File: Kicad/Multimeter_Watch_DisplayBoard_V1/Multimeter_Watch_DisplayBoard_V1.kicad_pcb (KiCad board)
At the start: 2 copper layers, 55 x 46 mm, 19 parts, among them J1 Conn_01x03_Male, J2 Conn_01x03_Male, J3 Conn_01x03_Male, J4 Conn_01x03_Male, Q1 A03400A N-MOS, SW1 SW_Push, SW2 SW_Push, SW3 SW_Push, SW4 SW_Push, SW5 SW_Push, SW6 SW_Push

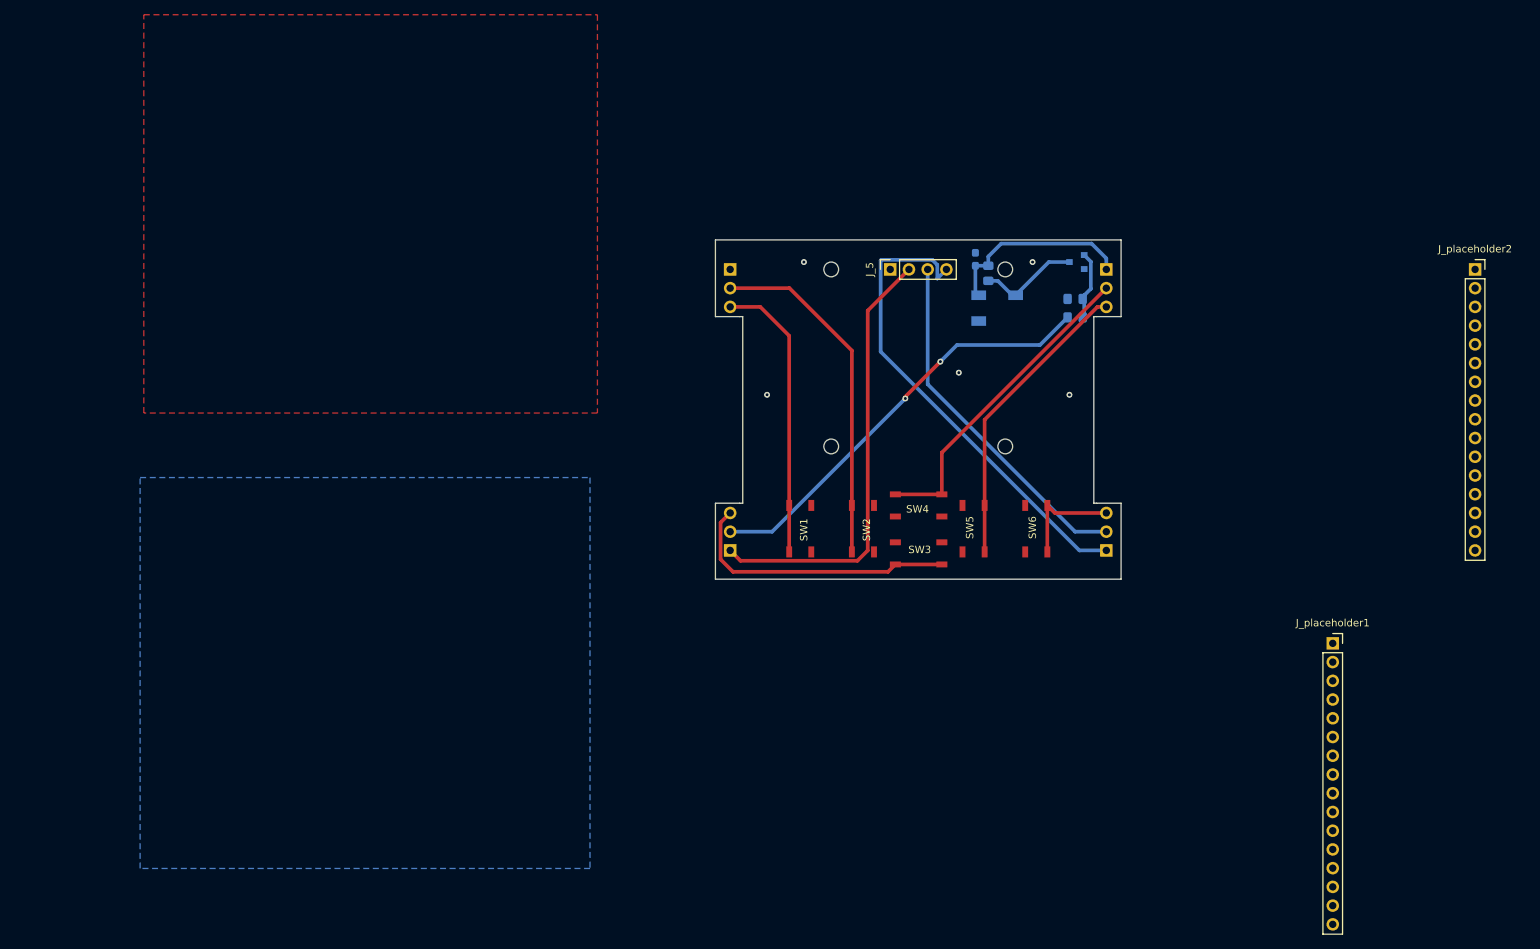
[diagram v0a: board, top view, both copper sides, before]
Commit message: display board laid out, added silkscreen desc. of pins and jacks
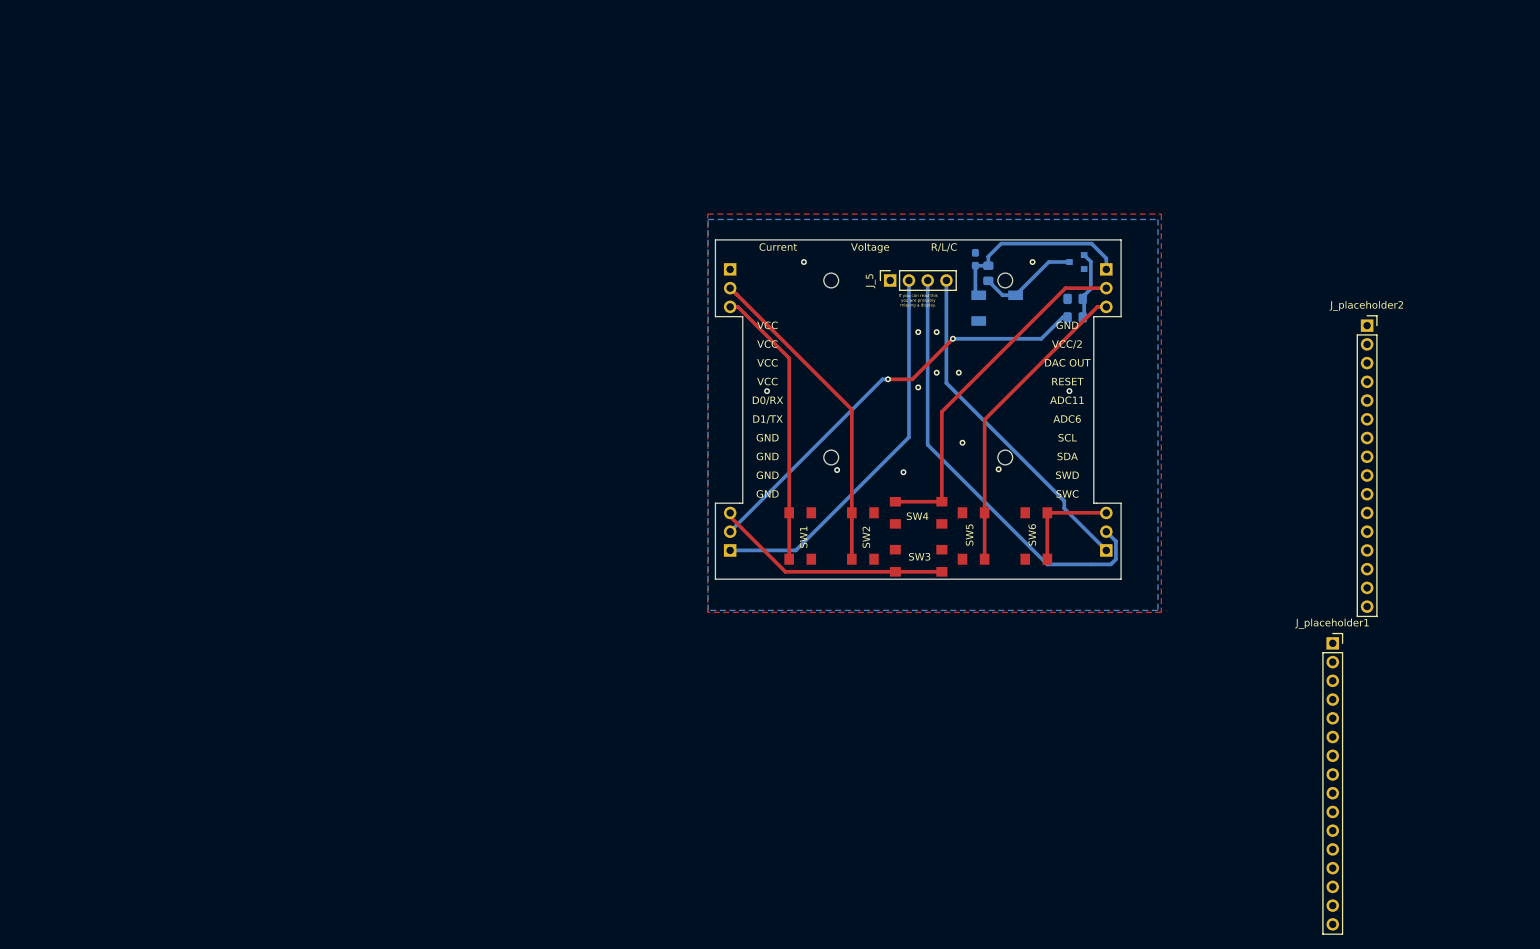
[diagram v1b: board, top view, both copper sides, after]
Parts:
- moved J_placeholder2 16.5 mm to (192.4, 66.6)
- moved J_5 1.50 mm to (127.7, 60.5)
- moved SW1 1.00 mm to (115.5, 95.2)
- moved SW2 1.00 mm to (124.0, 95.2)
- moved SW3 1.00 mm to (131.6, 98.5)
- moved SW4 1.00 mm to (131.5, 92.0)
- moved SW5 1.00 mm to (139.0, 95.1)
- moved SW6 1.00 mm to (147.5, 95.1)
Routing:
- net /SDA: track 65.7 -> 45.6 mm
- net /SCL: track 48.1 -> 59.1 mm
- net /ENABLE: track 60.2 -> 51.9 mm
- net /BUTT3: track 37.9 -> 32.3 mm
- net /BUTT4: track 43.5 -> 47.7 mm
- net /BUTT1: track 47.3 -> 43.6 mm, vias 0 -> 1
- net /BUTT5: track 40.8 -> 41.8 mm
- net /BUTT2: track 38.9 -> 38.1 mm
- net /GND: vias 5 -> 12
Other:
- outline, holes or cut-outs redrawn
- board text added: "ADC11"
- board text added: "ADC6"
- board text added: "Current"
- board text added: "D0/RX"
- board text added: "D1/TX"
- board text added: "DAC OUT"
- board text added: "GND"
- board text added: "If you can read this you are probably missing a display."
- board text added: "R/L/C"
- board text added: "RESET"
- board text added: "SCL"
- board text added: "SDA"
- board text added: "SWC"
- board text added: "SWD"
- board text added: "VCC"
- board text added: "VCC/2"
- board text added: "Voltage"

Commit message: add github, nouth and TGH logos
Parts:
- added G***: LOGO, Multimeter_Watch_custom_footprints:github_logo, F.Cu at (151.0, 57.0)
- added G***: LOGO, Multimeter_Watch_custom_footprints:nouth_signature, B.Cu at (131.6, 72.5)
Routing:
- net /SCL: vias 0 -> 1
- net /GND: vias 12 -> 13
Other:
- board text added: "8<:V>3"
- board text added: "ptrbroz/Multimeter_watch"

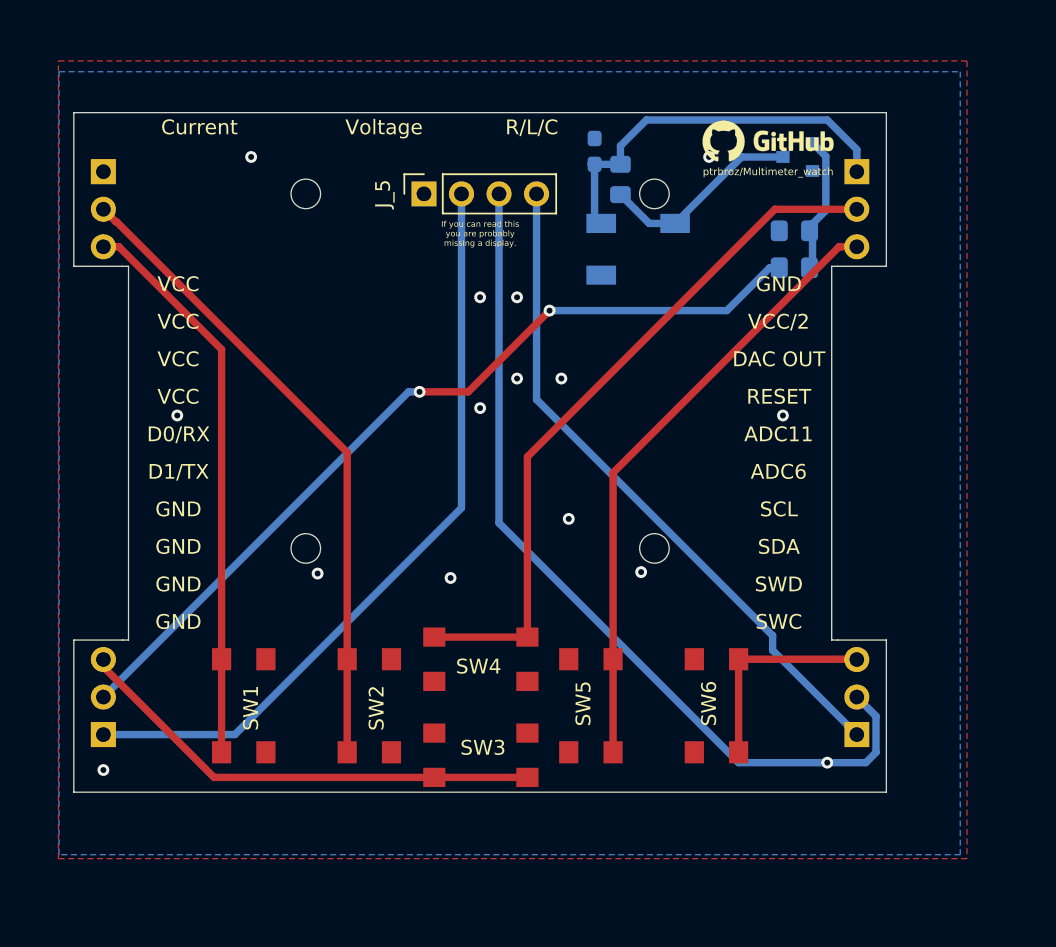
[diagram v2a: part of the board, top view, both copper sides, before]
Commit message: ground plane around crystal, silkscreen adjustments
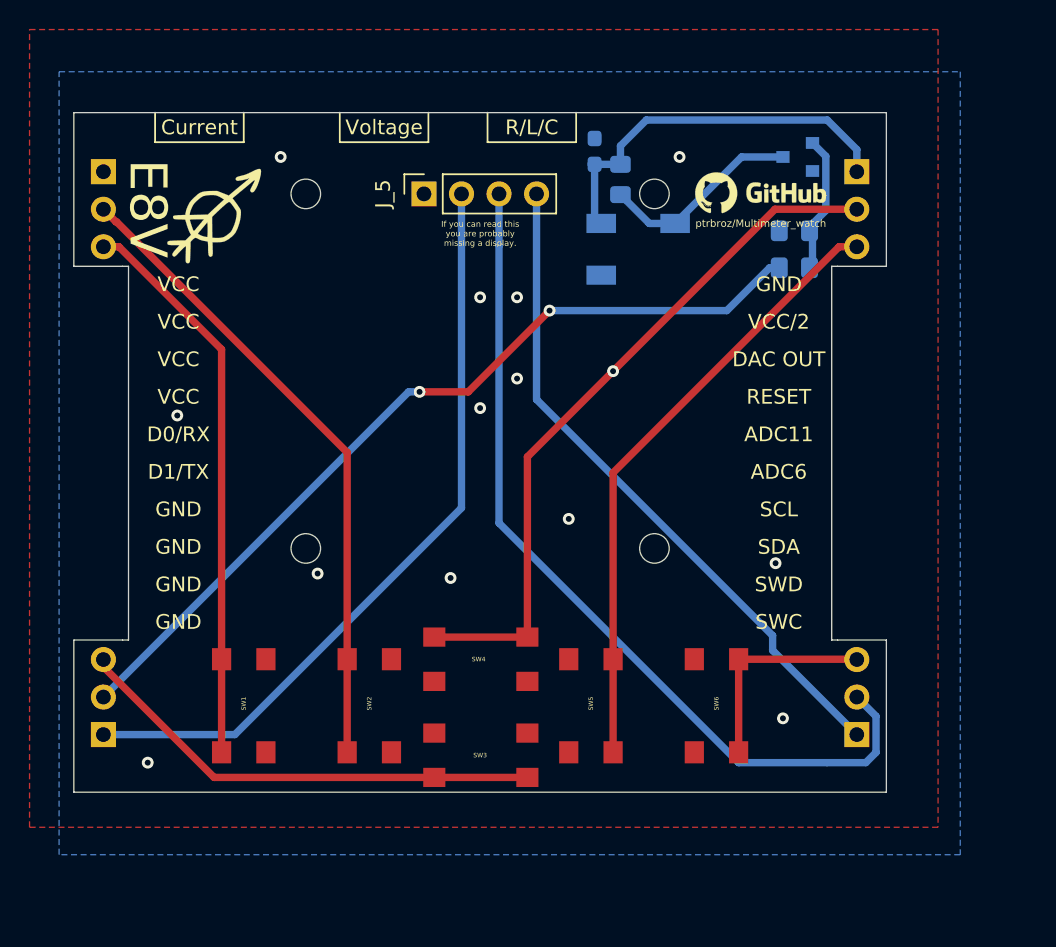
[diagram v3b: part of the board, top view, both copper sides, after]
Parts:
- G***: moved to F.Cu
- moved G*** 20.9 mm to (113.5, 62.0), turned to 0 degrees
- moved G*** 3.54 mm to (150.5, 60.5)
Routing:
- net /SCL: vias 1 -> 0
- net /BUTT4: vias 0 -> 1
- net /BUTT1: vias 1 -> 0
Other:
- board text added: "E8V"
- board text removed: "8<:V>3"
